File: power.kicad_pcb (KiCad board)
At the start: 2 copper layers, 99.7 x 100.3 mm, 212 parts, among them J1 USB_A, J2 Barrel_Jack_Switch, J3 Conn_02x06_Odd_Even, J4 Conn_02x10_Odd_Even, J5 Conn_02x06, J6 Conn_02x10_Odd_Even, J7 Conn_Coaxial, J8 Conn_Coaxial, Q1 MOSFET_P, T1 BALUN, T2 BALUN, U1 ZLDO1117G33TA, U10 lx9_XC6SLX9-TQ144, U11 FSM1LPTR, U12 FSM1LPTR, U13 FSM1LPTR, U14 SI5351C, U15 MAX5864, U16 MAX2830, U2 ZLDO1117G33TA, U3 ZLDO1117G33TA, U4 FSM1LPTR, U5 STM32F722ZET, U6 LSM9DS1, U7 Omega2+, U8 FSM1LPTR, U9 CY7C199, X1 Oscillator_ASE-xxxMHz, Y1 ABM8G-16.000MHZ-B4Y-T, Y2 Crystal, Y3 ABM8G-25.000MHZ-B4Y-T

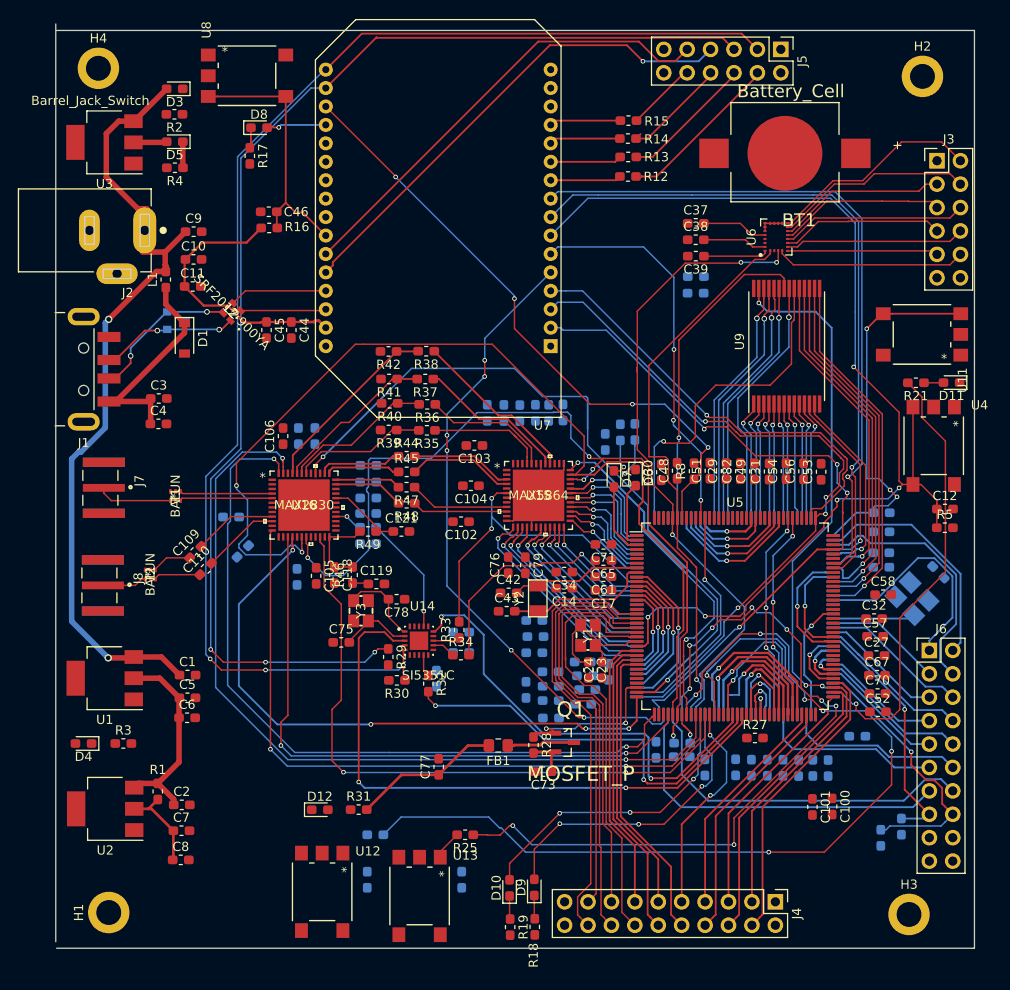
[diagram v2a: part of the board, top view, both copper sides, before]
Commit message: diseño de esquematico arreglo de flechas rojas
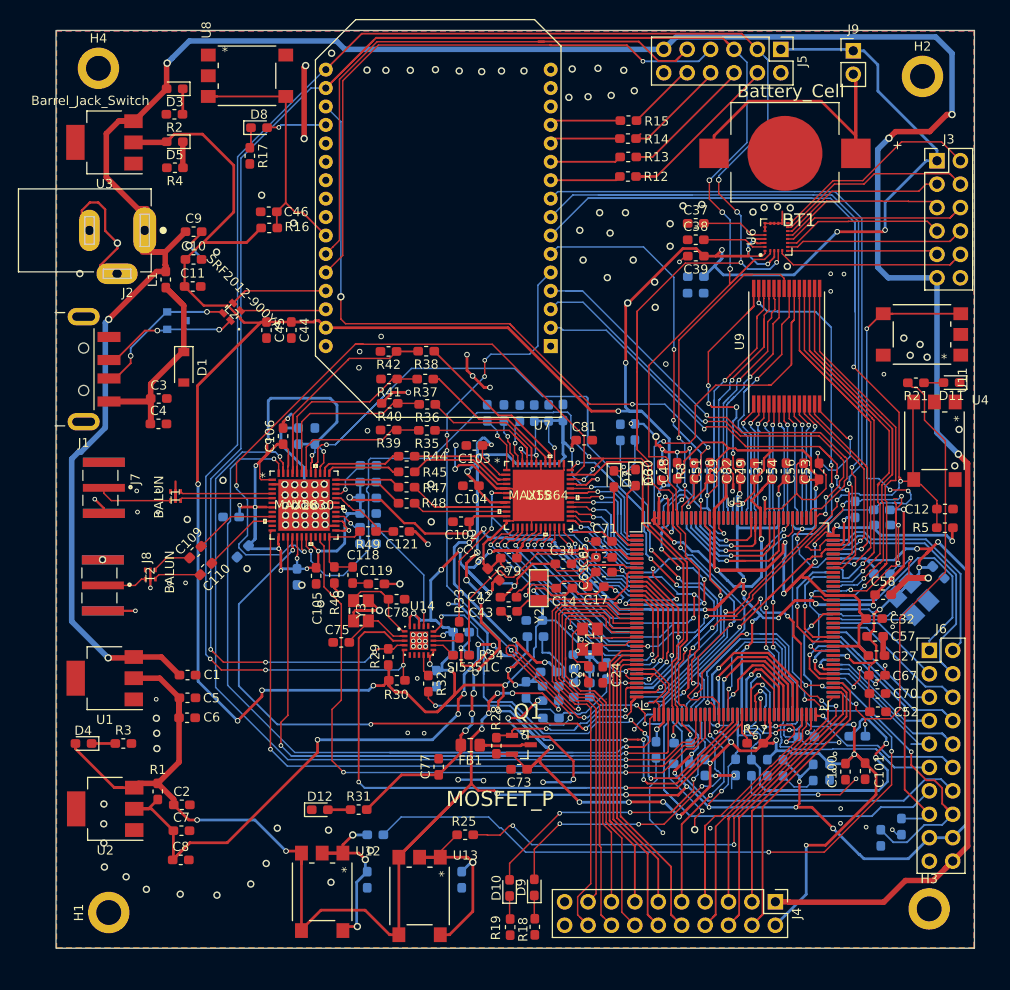
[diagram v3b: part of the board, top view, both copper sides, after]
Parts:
- removed C68: 0.47uF, Capacitor_SMD:C_0603_1608Metric_Pad1.05x0.95mm_HandSolder
- added J9: Conn_01x02_Male, Connector_PinHeader_2.54mm:PinHeader_1x02_P2.54mm_Vertical, F.Cu at (137.7, 17.4)
- C81: moved to F.Cu
- moved C101 6.91 mm to (139.0, 95.6), turned to 90 degrees
- moved C15 5.50 mm to (137.9, 67.2), turned to 90 degrees
- moved Q1 4.70 mm to (101.7, 92.7)
- moved C100 4.05 mm to (136.9, 95.7), turned to 90 degrees
- moved R28 4.03 mm to (99.0, 92.8)
- moved C13 3.48 mm to (132.6, 91.9), turned to 180 degrees
- moved D1 3.15 mm to (65.1, 51.8)
- moved FB1 3.04 mm to (96.2, 92.8)
- moved C73 2.64 mm to (101.5, 95.4)
- moved C81 2.30 mm to (108.5, 59.7), turned to 0 degrees
- moved H3 2.27 mm to (146.0, 110.5)
- moved C79 1.95 mm to (100.4, 72.5), turned to 180 degrees
- moved C76 1.90 mm to (98.7, 74.3), turned to 135 degrees
- moved Y2 1.11 mm to (103.6, 75.7)
- moved C20 0.93 mm to (108.3, 86.0)
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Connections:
- BT1 pad 1: vcc_STM32 -> Net-(BT1-Pad1)
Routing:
- net vcc_STM32: track 45.4 -> 703.4 mm, vias 0 -> 53
- net GND: track 22.8 -> 583.9 mm, vias 0 -> 221
- net vcc_FPGA: track 21.9 -> 471.7 mm, vias 0 -> 40
- net vcc_core_FPGA: track 9.86 -> 281.2 mm, vias 0 -> 26
- net VAA: track 16.1 -> 245.3 mm, vias 0 -> 29
- net VCC_5V: track 84.0 -> 301.3 mm, vias 2 -> 6
- net I2C_SCL: track 194.8 -> 283.3 mm, vias 4 -> 7
- net I2C_SDA: track 214.3 -> 261.8 mm, vias 6 -> 8
- net JNRST: track 122.6 -> 161.5 mm
- net Net-(BT1-Pad1): track 0.00 -> 37.4 mm
- net SPI1_CS_RF: track 67.8 -> 101.0 mm
- net GPIO_INTR: track 67.0 -> 95.2 mm
- net rf_RXTX: track 82.6 -> 104.8 mm
- net Net-(R23-Pad2): track 0.00 -> 20.8 mm, vias 0 -> 3
- net Net-(R24-Pad2): track 3.19 -> 23.0 mm, vias 0 -> 1
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- added copper zone on B.Cu, net GND
- added copper zone on F.Cu, net GND
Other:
- board size 99.7 x 100.3 mm -> 99.6 x 99.6 mm
- net class Default: clearance 0.2 -> 0.15
- rule trace_clearance: 0.2 -> 0.15

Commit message: Listo solo falta poner nombre
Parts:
- moved H4 1.34 mm to (57.1, 19.8)
- moved H3 1.22 mm to (144.8, 110.8)
- moved H1 0.70 mm to (56.7, 110.3)
- moved C64 0.27 mm to (140.8, 73.9)
- moved J1 0.25 mm to (47.6, 52.0)
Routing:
- net GND: track 583.9 -> 597.4 mm, vias 221 -> 284
- net vcc_STM32: track 703.4 -> 705.2 mm
- net VCC_5V: track 301.3 -> 303.0 mm
- net SPI1_SCK: track 124.4 -> 125.4 mm
- net vcc_FPGA: track 471.7 -> 472.2 mm, vias 40 -> 41
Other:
- outline, holes or cut-outs redrawn

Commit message: programacion luego del diseño del embebido
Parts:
- added C68: 0.47uF, Capacitor_SMD:C_0603_1608Metric_Pad1.05x0.95mm_HandSolder, F.Cu at (71.1, 87.8)
- C52, C72: value 0.1uf -> 0.1uF
- R16, R5: value 10K -> 10k
- R17, R18, R19, R2, R6, R7: value 600 -> 750
- R20, R21: value 220 -> 200
- R3, R4: value 330 -> 470
- U1, U2, U3: footprint Package_TO_SOT_SMD:SOT-223 -> Package_TO_SOT_SMD:SOT-223-3_TabPin2
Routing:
- net GND: track 597.4 -> 579.9 mm, vias 284 -> 300
- net vcc_FPGA: track 472.2 -> 483.1 mm
- net /FPGA_spartan6/FSW_2: track 91.1 -> 85.2 mm
- net JNRST: track 161.5 -> 155.7 mm
- net Net-(R38-Pad2): track 28.2 -> 22.8 mm
- net SPI1_CS_AD: track 49.7 -> 44.9 mm
- net vcc_core_FPGA: track 281.2 -> 285.8 mm
- net FMC_A6: track 29.8 -> 26.3 mm
- net /ONION_OMEGA/TX_PIN: track 62.2 -> 60.2 mm
- net JTMS: track 87.5 -> 85.7 mm
- net /STM32_micro/GPIO_11: track 50.6 -> 52.3 mm
- net vcc_STM32: track 705.2 -> 706.3 mm, vias 53 -> 55
- net /STM32_micro/GPIO_13: track 62.9 -> 64.0 mm
- net FMC_A7: track 22.4 -> 21.4 mm
- net Net-(C13-Pad1): track 5.50 -> 4.74 mm
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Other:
- board text added: "Eder Fabian Ruiz A edruiza@unal.edu.co"
